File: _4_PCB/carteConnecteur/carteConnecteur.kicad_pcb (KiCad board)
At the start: 2 copper layers, 17 parts, among them P1 +5 (ubec), P10 N.U, P11 I2c, P2 PAP_D, P3 +5 (pap_G), P4 +5 (pap_D), P5 PAP_G, P6 RPi_Conn, P7 +5 (sonar), P8 +5 (RPi)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

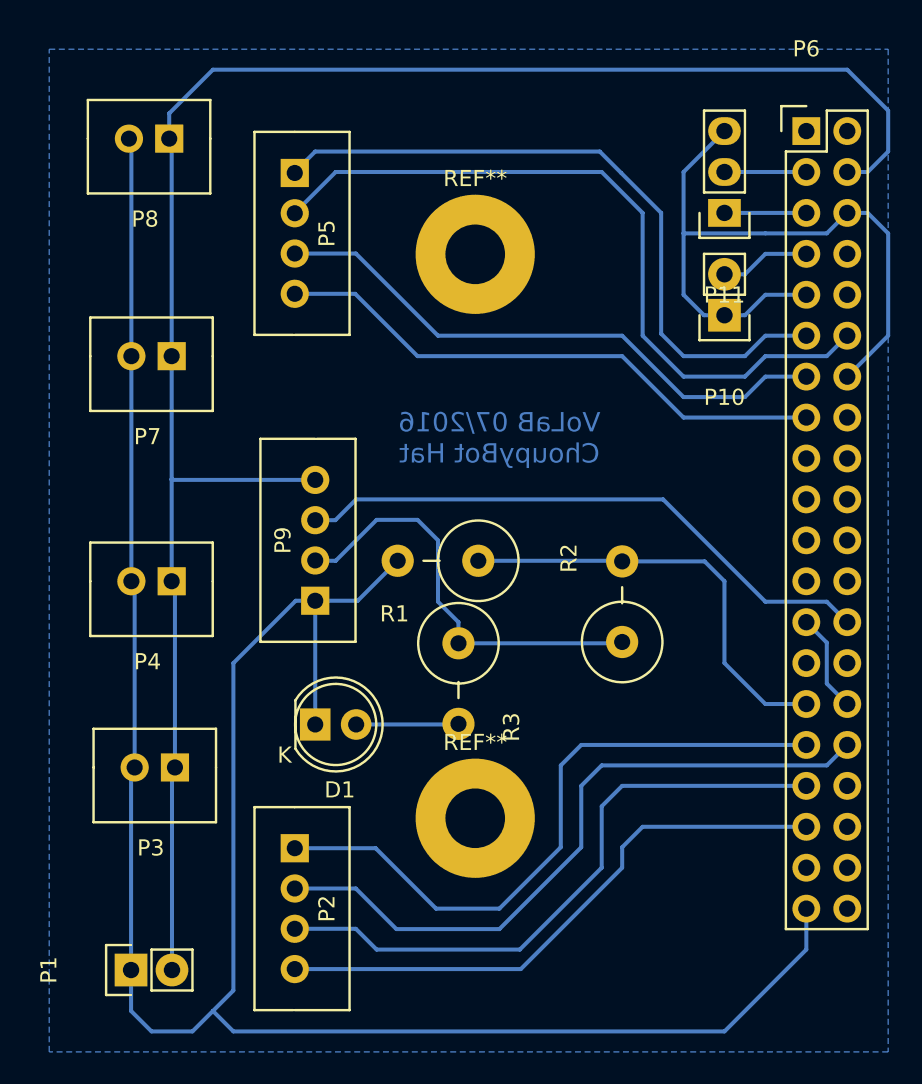
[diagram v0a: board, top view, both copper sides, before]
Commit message: ajout de 3 connecteur + pull-up sur le PCB + mise à jour des libs dans 'software'
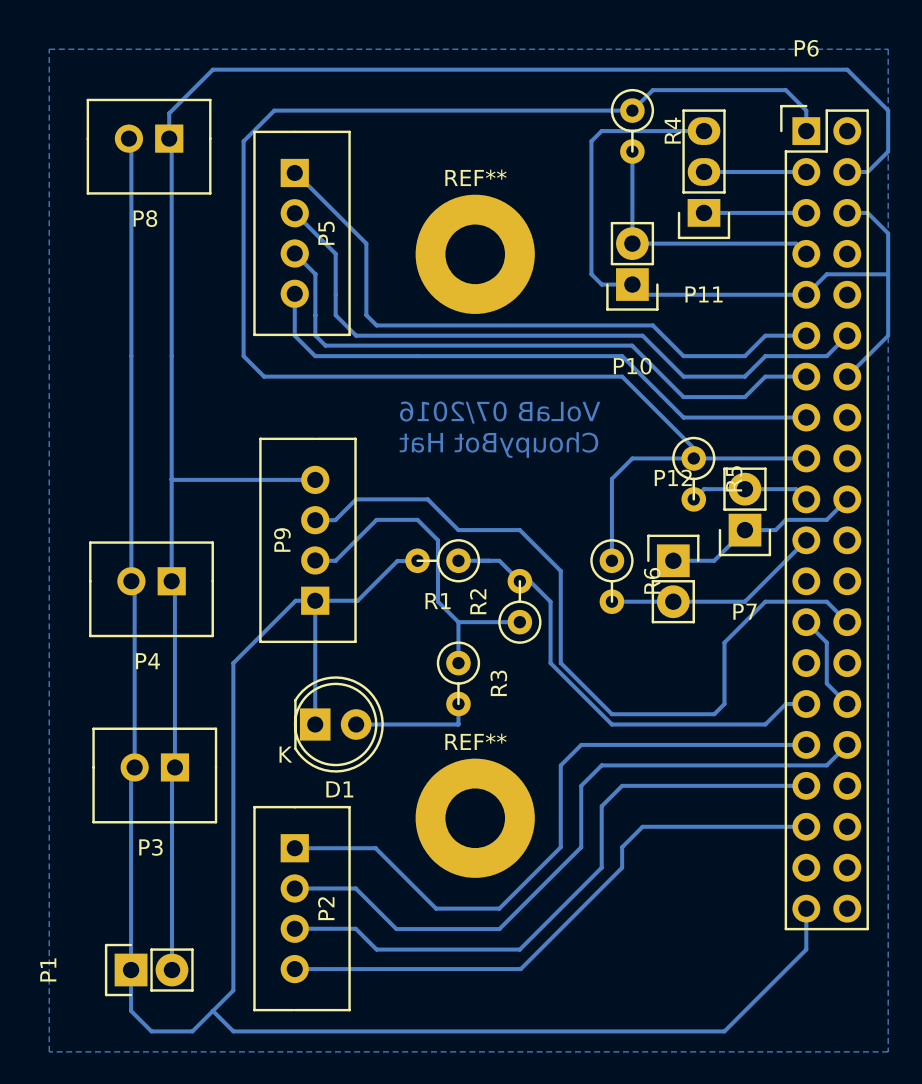
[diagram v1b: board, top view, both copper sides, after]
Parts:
- added P12: BP2, Pin_Headers:Pin_Header_Straight_1x02, F.Cu at (137.8, 96.5)
- added R4: 10k, myLib:Resistor_Vertical_2-54, F.Cu at (135.3, 69.8)
- added R5: 10k, myLib:Resistor_Vertical_2-54, F.Cu at (139.1, 91.4)
- added R6: 10k, myLib:Resistor_Vertical_2-54, F.Cu at (134.0, 97.8)
- P7: value +5 (sonar) -> BP1; footprint XH_connector:XH_connector_2pins_Vert -> Pin_Headers:Pin_Header_Straight_1x02
- R1, R2, R3: footprint Resistors_ThroughHole:Resistor_Vertical_RM5mm -> myLib:Resistor_Vertical_2-54
- moved P7 38.4 mm to (142.2, 94.6)
- moved R2 6.35 mm to (128.3, 99.1)
- moved P10 6.02 mm to (135.3, 79.4)
- moved P11 1.27 mm to (139.7, 74.9)
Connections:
- P6 pad 1: Net-(P6-Pad1) -> +3V3
- P6 pad 17: Net-(P6-Pad17) -> +3V3
- P7 pad 1: VCC -> GNDPWR
- P7 pad 2: GNDPWR -> Net-(P6-Pad19)
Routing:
- net +3V3: track 0.00 -> 100.0 mm
- net GNDPWR: track 194.8 -> 213.5 mm
- net Net-(P12-Pad2): track 0.00 -> 13.6 mm
- net /Trig: track 36.7 -> 48.1 mm
- net /GPIO04: track 5.61 -> 16.8 mm
- net Net-(P6-Pad19): track 0.00 -> 7.51 mm
- net /Echo: track 26.3 -> 21.2 mm
- net /GPIO18: track 46.1 -> 41.8 mm
- net /GPIO17: track 42.5 -> 39.6 mm
- net /GPIO27: track 36.0 -> 38.2 mm
- net Net-(P6-Pad29): track 27.0 -> 29.2 mm
- net /GPIO22: track 34.9 -> 36.5 mm
- net Net-(D1-Pad2): track 6.37 -> 7.71 mm
- net /SDA: track 5.08 -> 6.35 mm
- net /SCL: track 5.08 -> 6.35 mm
